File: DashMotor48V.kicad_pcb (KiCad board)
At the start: 6 copper layers, 72 x 69.7 mm, 86 parts, among them CN3(OUT)1 XT30(2+2)PB-M.G.B, CN3(OUT)2 XT30(2+2)PB-M.G.B, J1 BM07B-SRSS-TB, J2 BM07B-SRSS-TB, Q1 FDMS039N08B, Q2 FDMS039N08B, Q3 FDMS039N08B, Q4 FDMS039N08B, Q5 FDMS039N08B, Q6 FDMS039N08B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

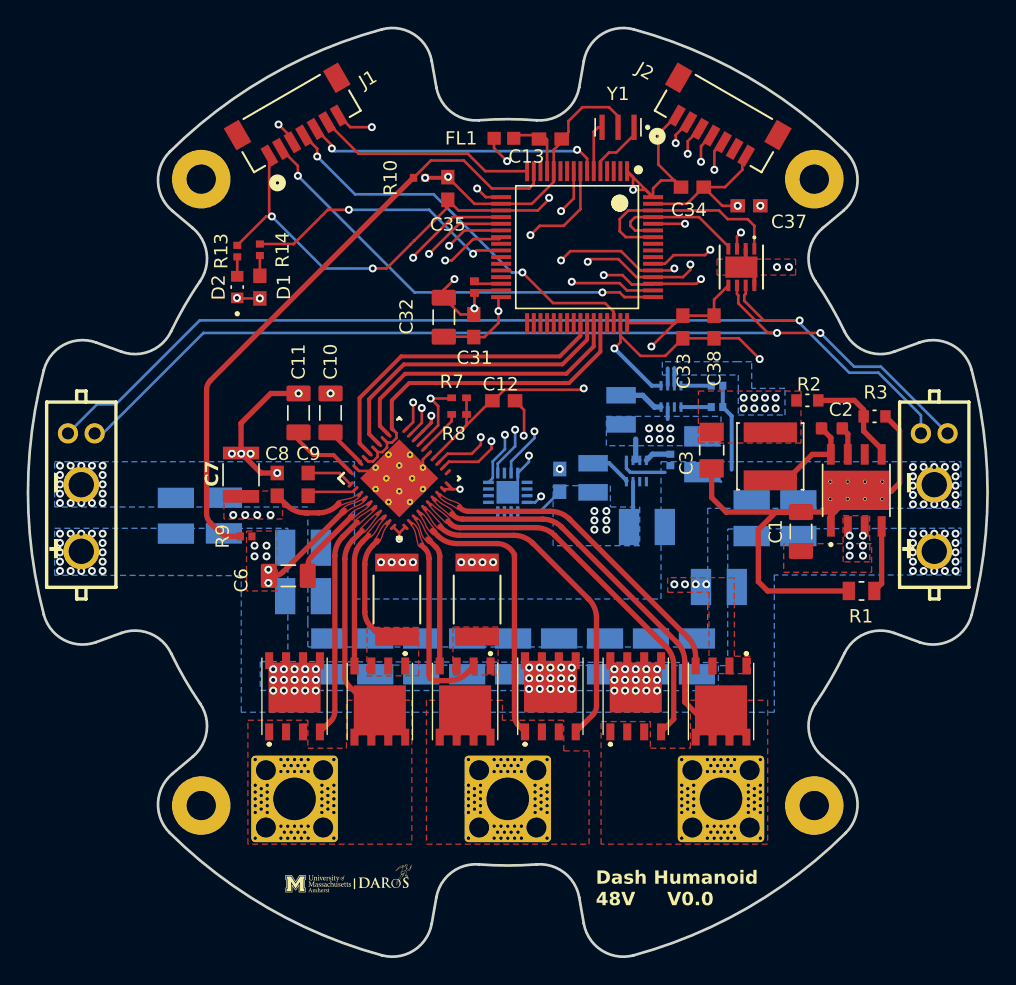
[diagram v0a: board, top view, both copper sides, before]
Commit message: need to add testing probe
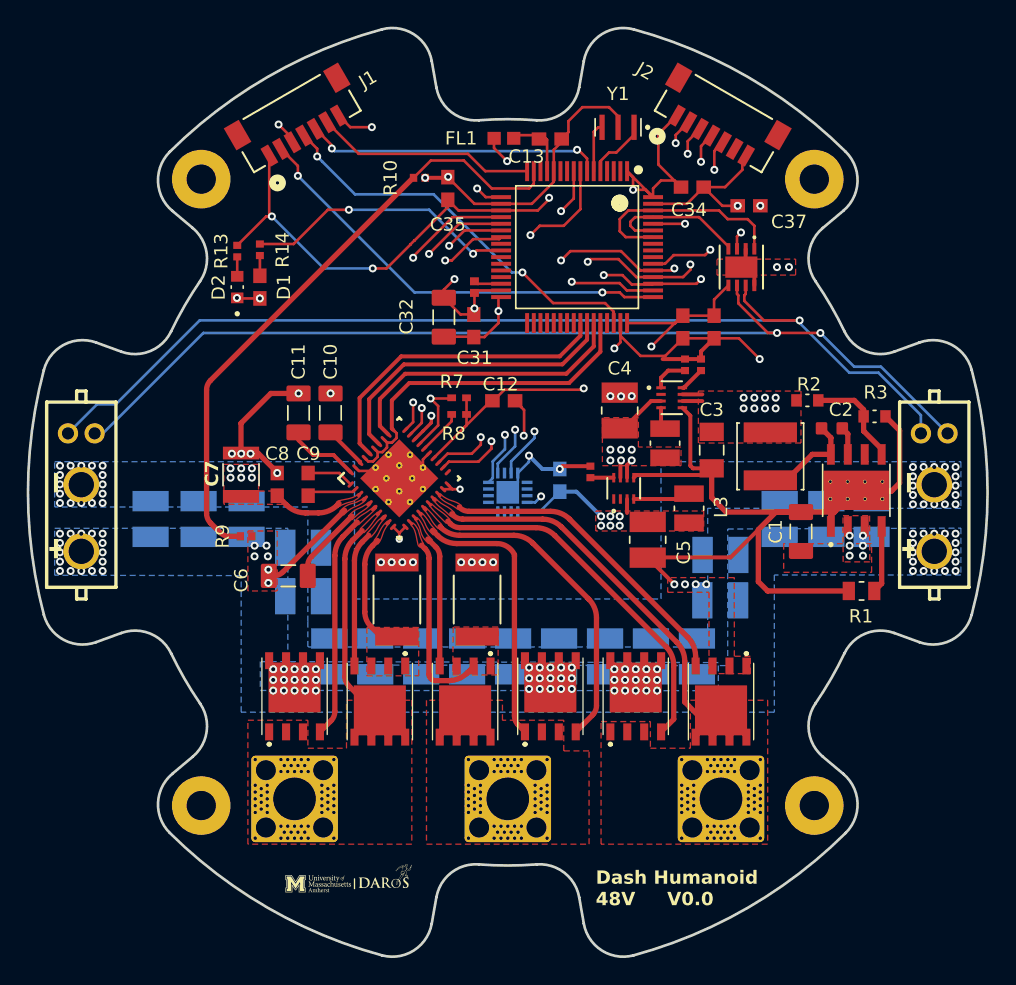
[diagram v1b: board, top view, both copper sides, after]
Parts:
- removed ?: , 
- added C39: 10uF, dash:GRM32EC72A106KE05L, B.Cu at (20.4, 2.00)
- added C40: 10uF, dash:GRM32EC72A106KE05L, B.Cu at (16.0, 4.70)
- added C41: 10uF, dash:GRM32EC72A106KE05L, B.Cu at (-19.6, 2.00)
- C4, C5, L2, L3, R4, R5, R6, U1, U2: moved to F.Cu
- moved L3 7.55 mm to (13.6, 1.19)
- moved C4 7.02 mm to (8.40, -6.14), turned to -90 degrees
- moved R6 6.07 mm to (6.20, -1.53), turned to -90 degrees
- moved C29 5.60 mm to (23.9, 2.00)
- moved C28 5.50 mm to (27.3, 2.00)
- moved L2 4.14 mm to (11.8, -3.69)
- moved R5 3.97 mm to (13.3, -9.57), turned to -90 degrees
- moved R4 1.97 mm to (14.5, -9.57), turned to -90 degrees
- moved C25 1.92 mm to (-23.2, 2.00)
- moved C24 1.92 mm to (-26.8, 2.00)
- moved U1 1.61 mm to (8.70, -0.30)
- moved C30 1.00 mm to (15.9, 8.10)
- moved C5 0.96 mm to (10.5, 3.56), turned to 90 degrees
- moved U2 0.11 mm to (12.3, -7.10), turned to 0 degrees
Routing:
- net GND: track 142.3 -> 160.6 mm, vias 68 -> 71
- net +5V: track 4.35 -> 8.07 mm
- net +3.3V: track 120.7 -> 123.3 mm
- net +12V: track 54.2 -> 56.0 mm, vias 12 -> 14
- net Net-(U2-SW): track 3.36 -> 1.77 mm
- net Net-(U1-SW): track 3.13 -> 4.32 mm
- net Net-(U2-FB/VSET): track 2.27 -> 2.77 mm
- added copper zone on F.Cu, net +3.3V
- added copper zone on F.Cu, net +5V
- removed copper zone on B.Cu, net +12V
- removed copper zone on B.Cu, net +3.3V
- removed copper zone on B.Cu, net +5V

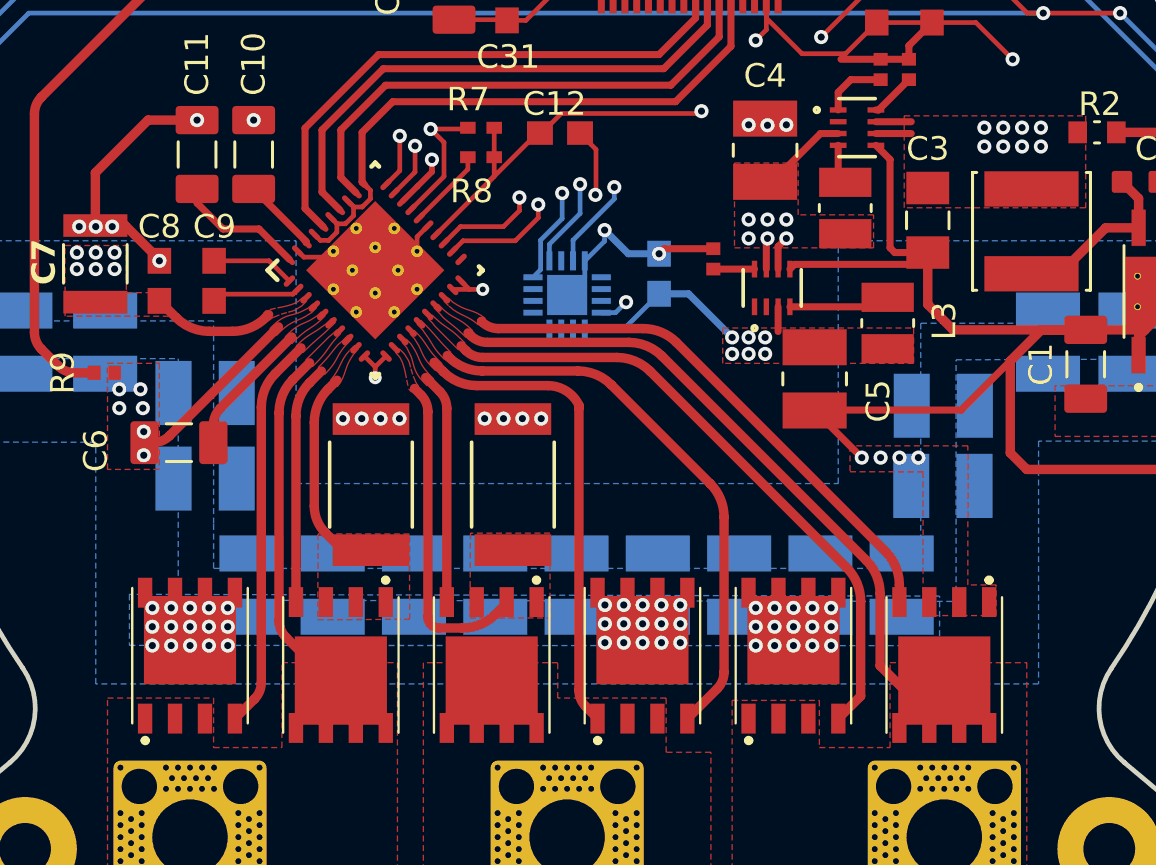
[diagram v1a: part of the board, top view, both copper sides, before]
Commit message: change a smaller shunt resistor and add more ground vias
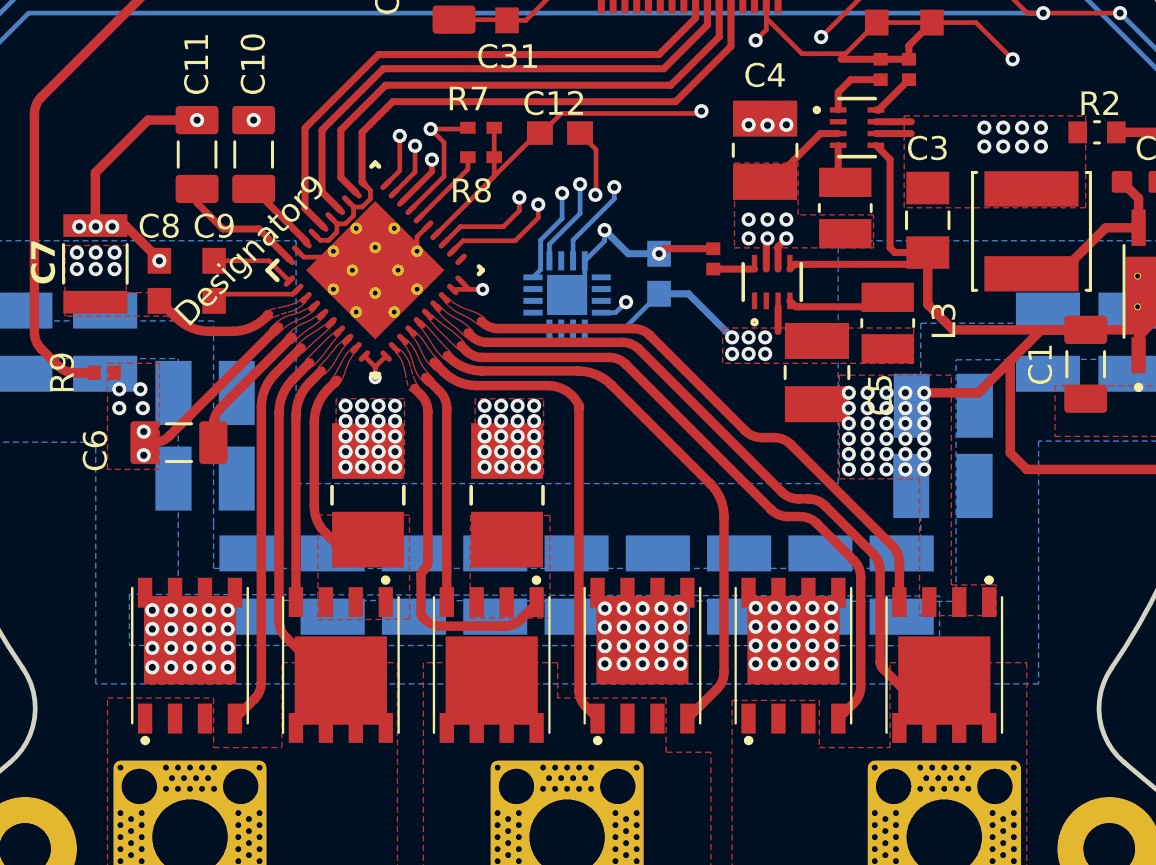
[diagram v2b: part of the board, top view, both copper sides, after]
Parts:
- R11, R12: value WSLF25121L000FEA -> WSLP20101L000FEA; footprint dash:WSLF25121L000FEA -> dash:WSLP20101L000FEA
- moved R12 0.52 mm to (-2.55, 8.50)
- moved R11 0.47 mm to (-8.45, 8.50)
- moved C5 0.29 mm to (10.6, 3.29)
- moved U1 0.25 mm to (8.70, -0.55)
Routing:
- net GND: track 160.6 -> 153.3 mm, vias 71 -> 129
- net +12V: track 56.0 -> 60.9 mm
- net /SPB: track 13.8 -> 15.4 mm
- net +48V: vias 89 -> 104

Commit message: increase ground and 48v copper pour on layer six
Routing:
- net +3.3V: vias 14 -> 15
- net +5V: vias 8 -> 10
- net +48V: vias 104 -> 128
- net +12V: vias 14 -> 16
